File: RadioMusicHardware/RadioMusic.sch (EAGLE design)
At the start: 62 parts, among them IC2 7805L, IC3 TL072P, IC4 TL072P

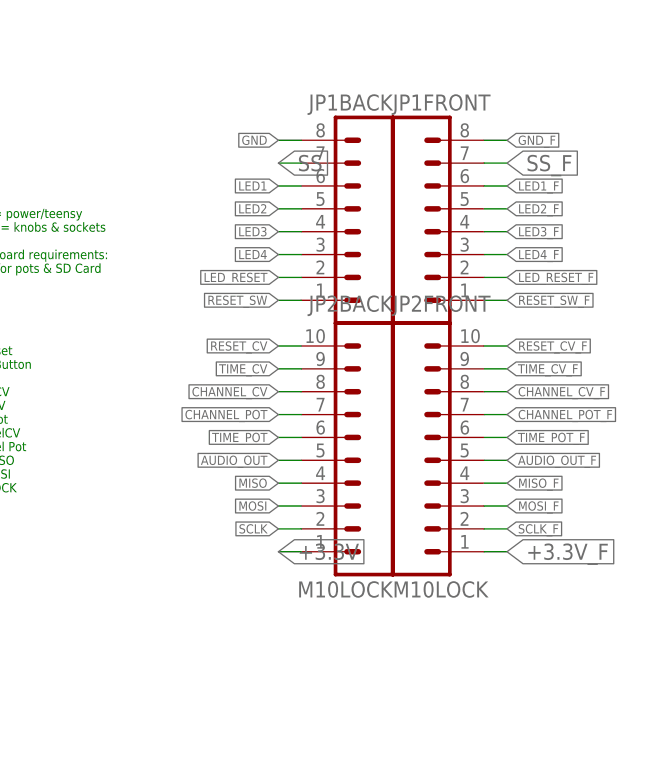
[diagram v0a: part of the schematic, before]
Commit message: First autorouted board
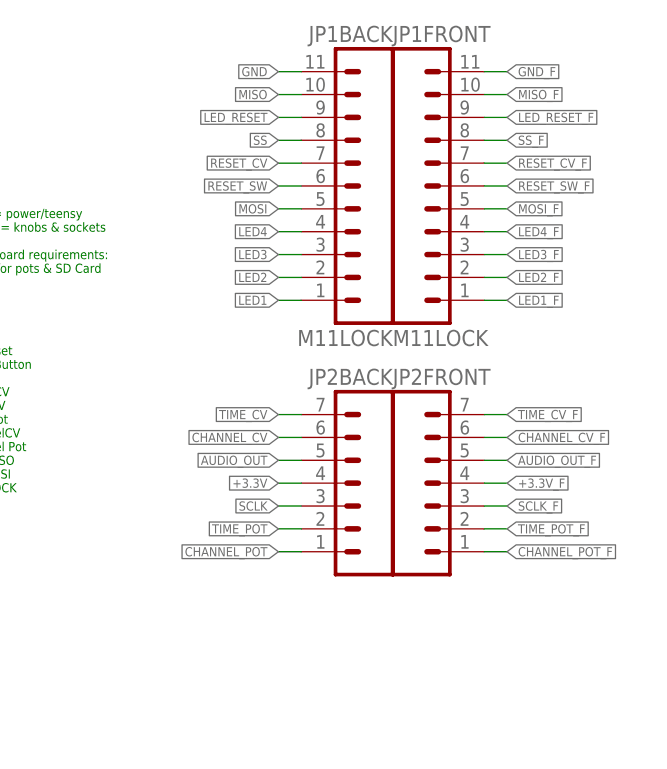
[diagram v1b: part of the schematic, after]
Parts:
- JP1BACK, JP1FRONT: value (none) -> M11LOCK; device SparkFun-Connectors:M08LOCK -> SparkFun-Connectors:M11LOCK
- JP2BACK, JP2FRONT: value M10LOCK -> (none); device SparkFun-Connectors:M10LOCK -> SparkFun-Connectors:M07LOCK
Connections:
- net +3.3V: now also JP2BACK.4; no longer JP2BACK.1
- net +3.3V_F: now also JP2FRONT.4; no longer JP2FRONT.1
- net CHANNEL_CV: now also JP2BACK.6; no longer JP2BACK.8
- net CHANNEL_CV_F: now also JP2FRONT.6; no longer JP2FRONT.8
- net CHANNEL_POT: now also JP2BACK.1; no longer JP2BACK.7
- net CHANNEL_POT_F: now also JP2FRONT.1; no longer JP2FRONT.7
- net GND: now also JP1BACK.11; no longer JP1BACK.8
- net GND_F: now also JP1FRONT.11; no longer JP1FRONT.8
- net LED1: now also JP1BACK.1; no longer JP1BACK.6
- net LED1_F: now also JP1FRONT.1; no longer JP1FRONT.6
- net LED2: now also JP1BACK.2; no longer JP1BACK.5
- net LED2_F: now also JP1FRONT.2; no longer JP1FRONT.5
- net LED3: now also JP1BACK.3; no longer JP1BACK.4
- net LED3_F: now also JP1FRONT.3; no longer JP1FRONT.4
- net LED4: now also JP1BACK.4; no longer JP1BACK.3
- net LED4_F: now also JP1FRONT.4; no longer JP1FRONT.3
- net LED_RESET: now also JP1BACK.9; no longer JP1BACK.2
- net LED_RESET_F: now also JP1FRONT.9; no longer JP1FRONT.2
- net MISO: now also JP1BACK.10; no longer JP2BACK.4
- net MISO_F: now also JP1FRONT.10; no longer JP2FRONT.4
- net MOSI: now also JP1BACK.5; no longer JP2BACK.3
- net MOSI_F: now also JP1FRONT.5; no longer JP2FRONT.3
- net RESET_CV: now also JP1BACK.7; no longer JP2BACK.10
- net RESET_CV_F: now also JP1FRONT.7; no longer JP2FRONT.10
- net RESET_SW: now also JP1BACK.6; no longer JP1BACK.1
- net RESET_SW_F: now also JP1FRONT.6; no longer JP1FRONT.1
- net SCLK: now also JP2BACK.3; no longer JP2BACK.2
- net SCLK_F: now also JP2FRONT.3; no longer JP2FRONT.2
- net SS: now also JP1BACK.8; no longer JP1BACK.7
- net SS_F: now also JP1FRONT.8; no longer JP1FRONT.7
- net TIME_CV: now also JP2BACK.7; no longer JP2BACK.9
- net TIME_CV_F: now also JP2FRONT.7; no longer JP2FRONT.9
- net TIME_POT: now also JP2BACK.2; no longer JP2BACK.6
- net TIME_POT_F: now also JP2FRONT.2; no longer JP2FRONT.6

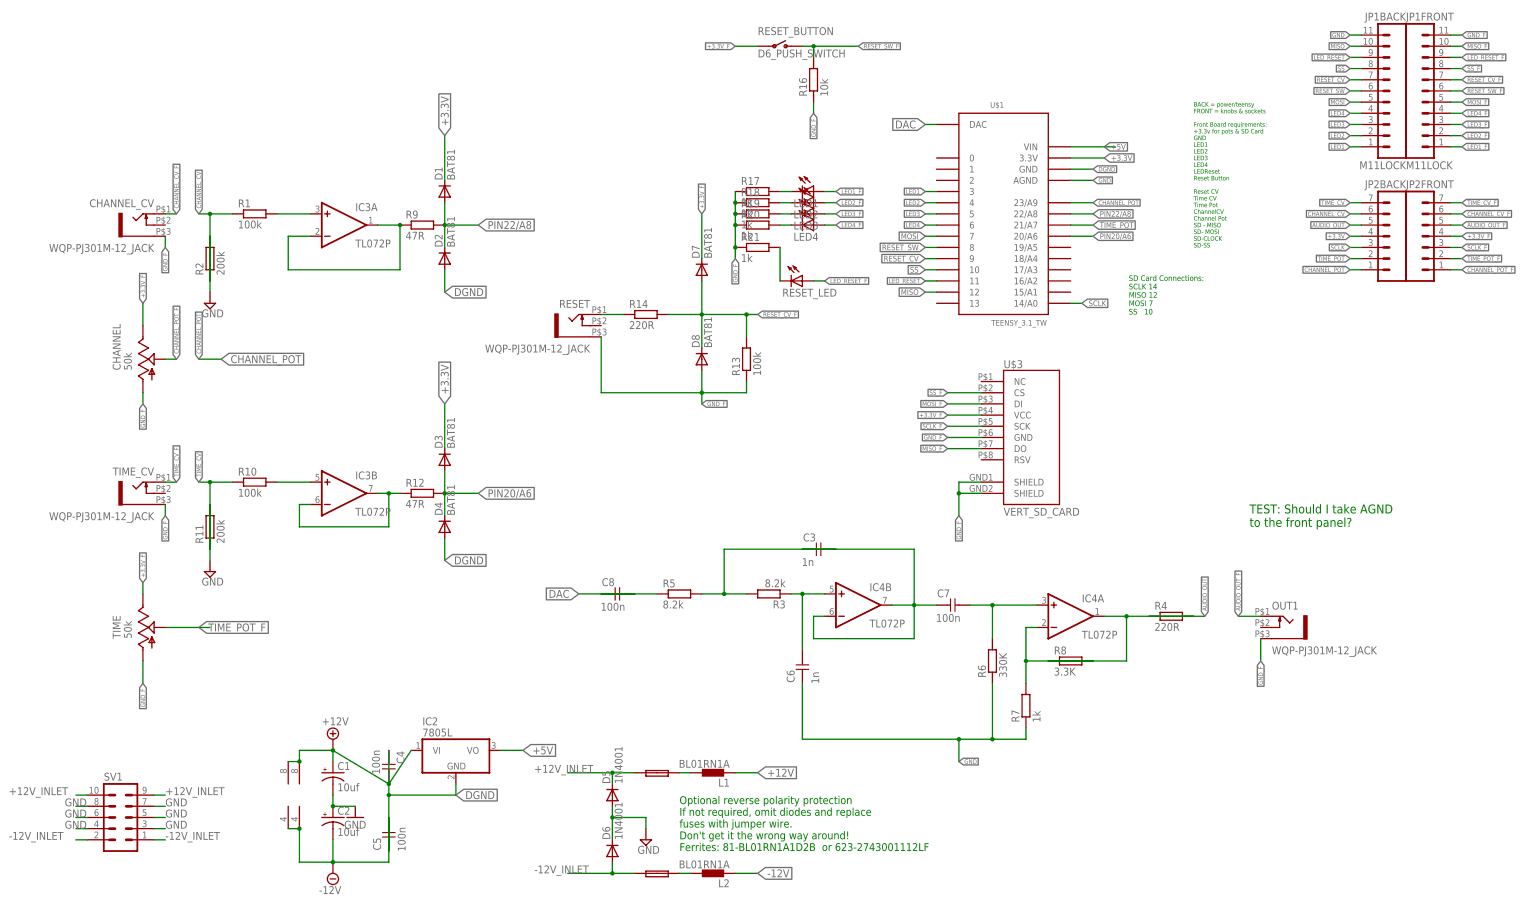
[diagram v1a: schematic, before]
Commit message: Add output level trim
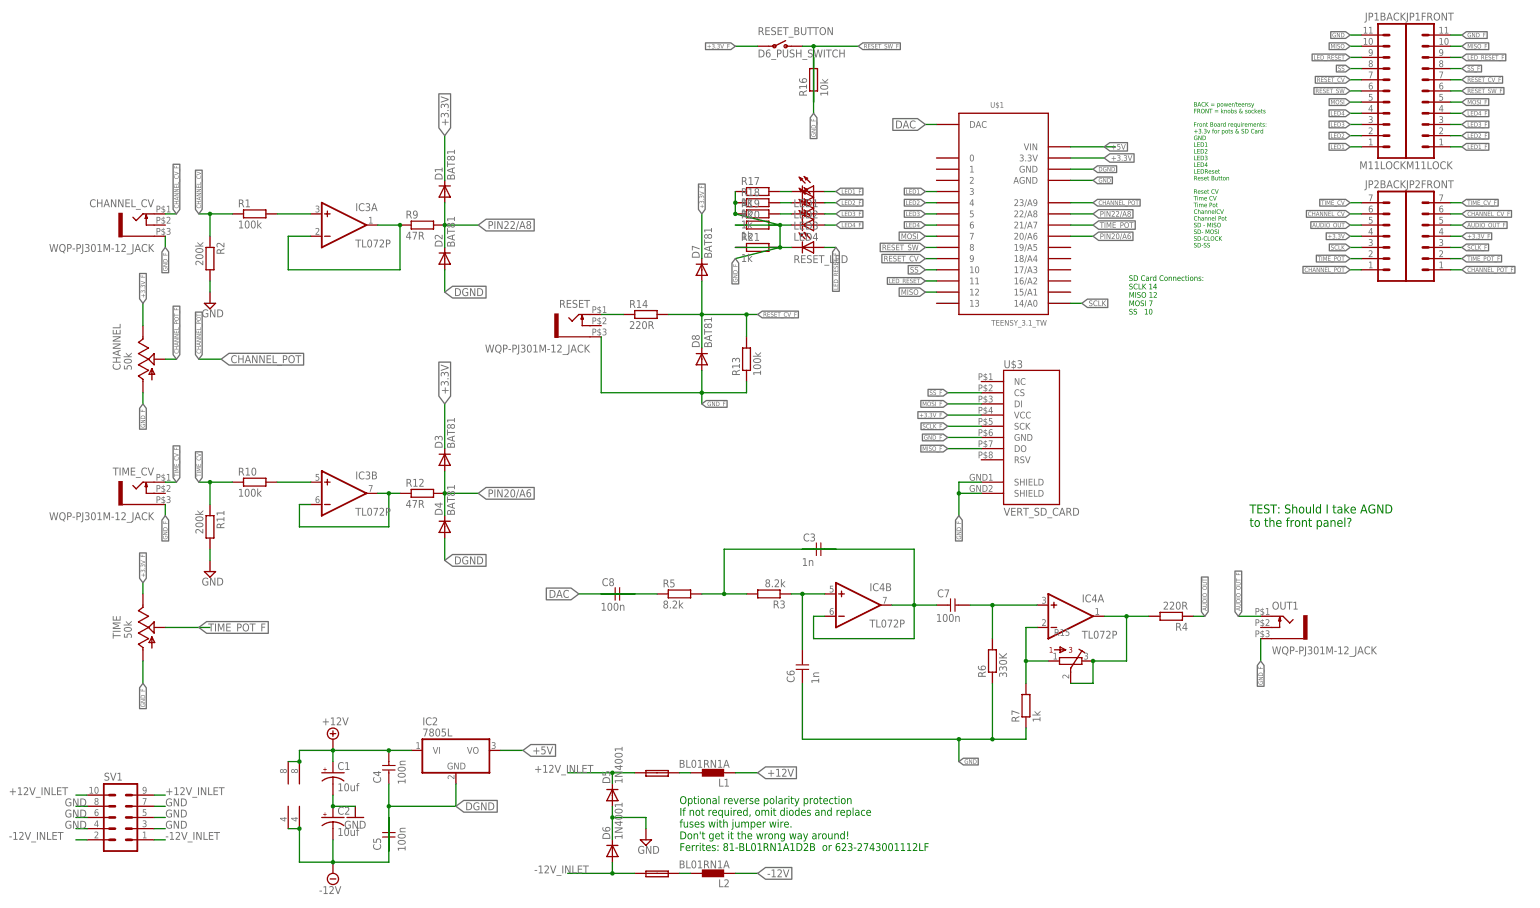
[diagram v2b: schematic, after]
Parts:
- removed R8: 3.3K, TomW:R-EU_STANDARD_RESISTOR
- added R15: (no value), bourns:3362P
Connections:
- net GND_F: now also R16.2, R20.2, R21.2; no longer R16.1, R20.1, R21.1
- net N$21: now also R20.1; no longer R20.2
- net N$25: now also R21.1; no longer R21.2
- net N$7: now also R15.1; no longer R8.2
- net N$8: now also R15.2, R15.3; no longer R8.1
- net RESET_SW_F: now also R16.1; no longer R16.2
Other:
- moved on the sheet: C4, R11, R2, R4, RESET_LED

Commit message: Add reset LED
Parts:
- renumbered R15 to VOLUME
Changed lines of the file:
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@@
 <part name="IC3" library="TomW" deviceset="TL072" device="P"/>
 <part name="IC4" library="TomW" deviceset="TL072" device="P"/>
-<part name="R15" library="bourns" deviceset="3362" device="P"/>
+<part name="VOLUME" library="bourns" deviceset="3362" device="P"/>
 </parts>
 <sheets>
@@
 <instance part="IC3" gate="P" x="53.34" y="27.94"/>
 <instance part="IC4" gate="P" x="55.88" y="27.94"/>
-<instance part="R15" gate="G$1" x="231.14" y="58.42" rot="R270"/>
+<instance part="VOLUME" gate="G$1" x="231.14" y="58.42" rot="R270"/>
 </instances>
 <busses>
@@
 <wire x1="226.06" y1="58.42" x2="220.98" y2="58.42" width="0.1524" layer="91"/>
 <junction x="220.98" y="58.42"/>
-<pinref part="R15" gate="G$1" pin="1"/>
+<pinref part="VOLUME" gate="G$1" pin="1"/>
 </segment>
 </net>
@@
 <wire x1="243.84" y1="58.42" x2="243.84" y2="68.58" width="0.1524" layer="91"/>
 <junction x="243.84" y="68.58"/>
-<pinref part="R15" gate="G$1" pin="3"/>
-<pinref part="R15" gate="G$1" pin="2"/>
+<pinref part="VOLUME" gate="G$1" pin="3"/>
+<pinref part="VOLUME" gate="G$1" pin="2"/>
 <wire x1="231.14" y1="53.34" x2="236.22" y2="53.34" width="0.1524" layer="91"/>
 <wire x1="236.22" y1="53.34" x2="236.22" y2="58.42" width="0.1524" layer="91"/>
